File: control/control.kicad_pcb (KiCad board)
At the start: 2 copper layers, 100 x 50 mm, 46 parts, among them J1 Conn_01x06_Male, J2 Conn_01x02_Male, Q1 TD9944, Q2 TD9944, Q3 TD9944, SW1 SW_SPST_X3, U1 Teensy_LC, U2 MCP3208, U3 74HC14

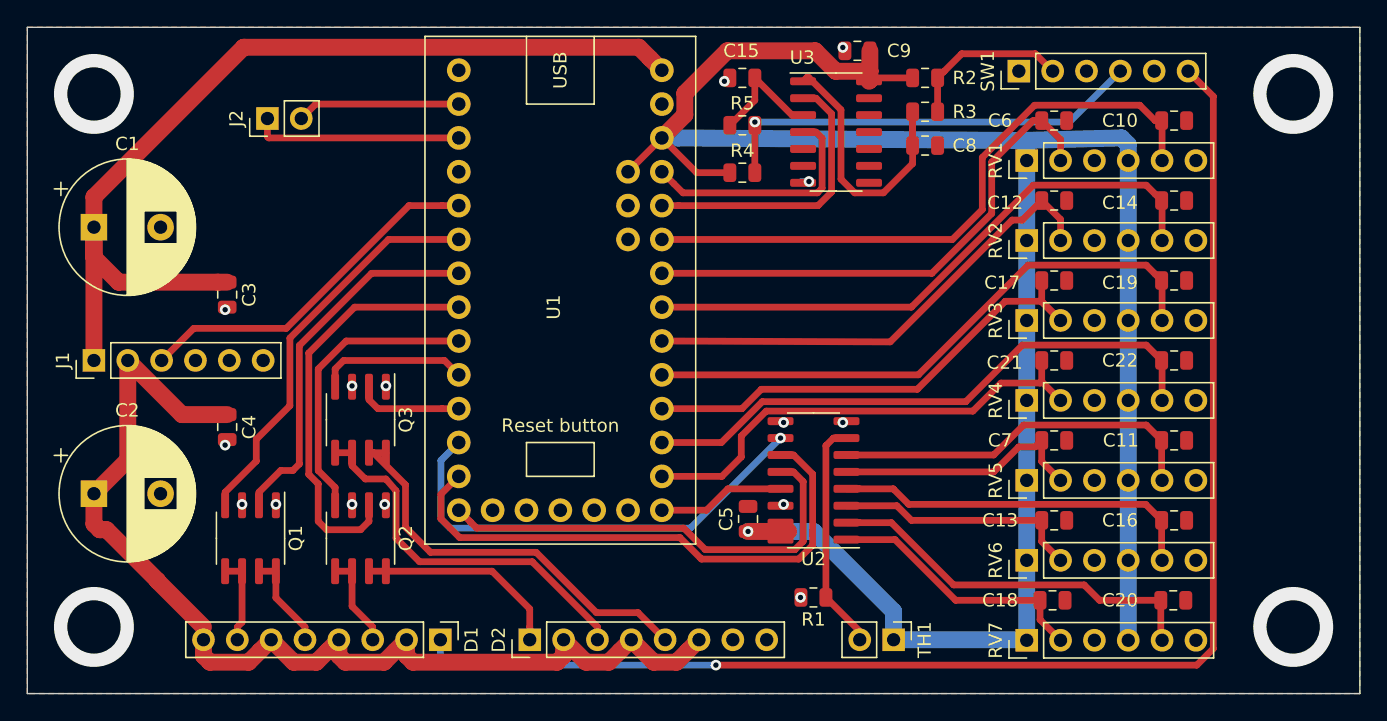
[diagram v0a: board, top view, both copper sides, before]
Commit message: Correction de pad non connecté
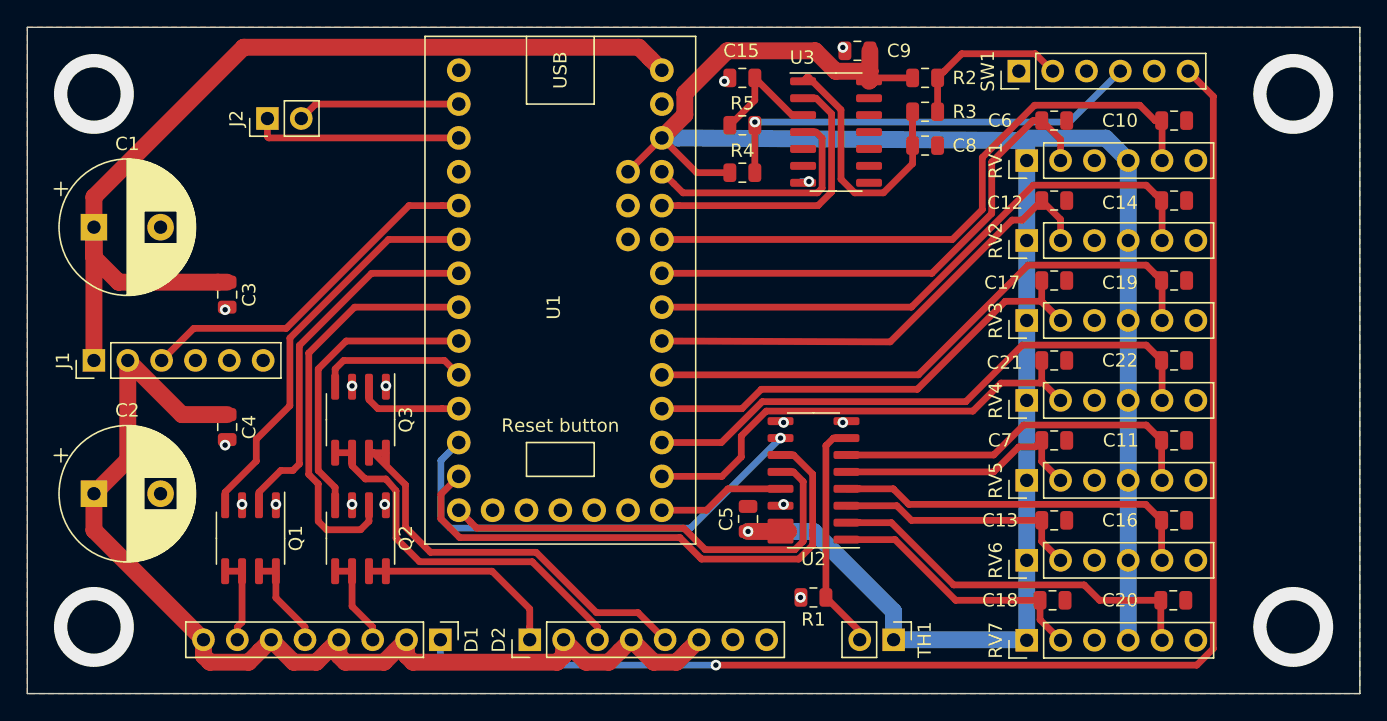
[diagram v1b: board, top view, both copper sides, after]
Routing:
- net D+12V: track 82.3 -> 82.9 mm
- net /MCU/3V3: track 174.1 -> 174.7 mm
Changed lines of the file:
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@@
     (thickness 1.6)
     (drawings 4)
-    (tracks 394)
+    (tracks 391)
     (zones 0)
     (modules 46)
@@
   (via (at 73.025 57.785) (size 0.8) (drill 0.4) (layers F.Cu B.Cu) (net 2))
   (segment (start 73.055 57.785) (end 73.025 57.785) (width 0.508) (layer F.Cu) (net 2))
-  (segment (start 28.22 60) (end 24.765 56.545) (width 1.27) (layer F.Cu) (net 3))
-  (segment (start 24.765 56.545) (end 24.765 56.515) (width 1.27) (layer F.Cu) (net 3))
-  (segment (start 24.765 56.515) (end 20.955 52.705) (width 1.27) (layer F.Cu) (net 3))
-  (segment (start 20 52.27) (end 20 50) (width 1.27) (layer F.Cu) (net 3))
-  (segment (start 20.435 52.705) (end 20 52.27) (width 1.27) (layer F.Cu) (net 3))
-  (segment (start 20.955 52.705) (end 20.435 52.705) (width 1.27) (layer F.Cu) (net 3))
   (segment (start 22.54 47.46) (end 22.54 40) (width 1.27) (layer F.Cu) (net 3))
   (segment (start 20 50) (end 22.54 47.46) (width 1.27) (layer F.Cu) (net 3))
@@
   (segment (start 63.719999 62.645001) (end 64.555001 61.809999) (width 1.27) (layer F.Cu) (net 3))
   (segment (start 60.325 60.96) (end 62.010001 62.645001) (width 1.27) (layer F.Cu) (net 3))
-  (segment (start 92.54 23.415) (end 91.125 22) (width 0.508) (layer F.Cu) (net 4))
-  (segment (start 92.54 25) (end 92.54 23.415) (width 0.508) (layer F.Cu) (net 4))
+  (segment (start 20 52.74) (end 20 50) (width 1.27) (layer F.Cu) (net 3))
+  (segment (start 28.22 60.96) (end 20 52.74) (width 1.27) (layer F.Cu) (net 3))
   (segment (start 91.125 22) (end 90.482798 22) (width 0.508) (layer F.Cu) (net 4))
   (segment (start 87.376 25.106798) (end 87.376 28.970724) (width 0.508) (layer F.Cu) (net 4))
@@
   (segment (start 82.886724 33.46) (end 62.62 33.46) (width 0.508) (layer F.Cu) (net 4))
   (segment (start 87.376 28.970724) (end 82.886724 33.46) (width 0.508) (layer F.Cu) (net 4))
+  (segment (start 92.54 23.415) (end 91.125 22) (width 0.508) (layer F.Cu) (net 4))
+  (segment (start 92.54 25) (end 92.54 23.415) (width 0.508) (layer F.Cu) (net 4))
   (segment (start 90.639473 46.485527) (end 89.404473 46.485527) (width 0.508) (layer F.Cu) (net 5))
   (segment (start 91.125 46) (end 90.639473 46.485527) (width 0.508) (layer F.Cu) (net 5))
@@
   (segment (start 97.62 31) (end 97.62 25) (width 1.27) (layer B.Cu) (net 51))
   (segment (start 63.877235 23.3) (end 62.62 23.3) (width 1.27) (layer B.Cu) (net 51))
-  (segment (start 97.62 23.797919) (end 97.122081 23.3) (width 1.27) (layer B.Cu) (net 51))
-  (segment (start 97.62 25) (end 97.62 23.797919) (width 1.27) (layer B.Cu) (net 51))
   (segment (start 90 23.96) (end 89.535 23.495) (width 1.27) (layer B.Cu) (net 51))
   (segment (start 90 25) (end 90 23.96) (width 1.27) (layer B.Cu) (net 51))
-  (segment (start 97.122081 23.3) (end 89.535 23.495) (width 1.27) (layer B.Cu) (net 51))
   (segment (start 89.535 23.495) (end 63.877235 23.3) (width 1.27) (layer B.Cu) (net 51))
   (segment (start 60.08 25.84) (end 62.62 23.3) (width 0.508) (layer F.Cu) (net 51))
@@
   (segment (start 78.22099 18.29901) (end 78.232 18.288) (width 1.27) (layer F.Cu) (net 51))
   (segment (start 78.232 16.764) (end 78.232 18.288) (width 1.27) (layer F.Cu) (net 51))
+  (segment (start 89.715001 23.314999) (end 89.535 23.495) (width 1.27) (layer B.Cu) (net 51))
+  (segment (start 95.934999 23.314999) (end 89.715001 23.314999) (width 1.27) (layer B.Cu) (net 51))
+  (segment (start 97.62 25) (end 95.934999 23.314999) (width 1.27) (layer B.Cu) (net 51))
+  (segment (start 71.525 52.175) (end 71.525 53.445) (width 0.508) (layer F.Cu) (net 51))
   (segment (start 63.508999 26.728999) (end 62.62 25.84) (width 0.508) (layer F.Cu) (net 53))
   (segment (start 64.20401 27.42401) (end 63.508999 26.728999) (width 0.508) (layer F.Cu) (net 53))

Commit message: Correciton du PCB (espacements entre les connecteurs et polygon pour pour l'ADC.)
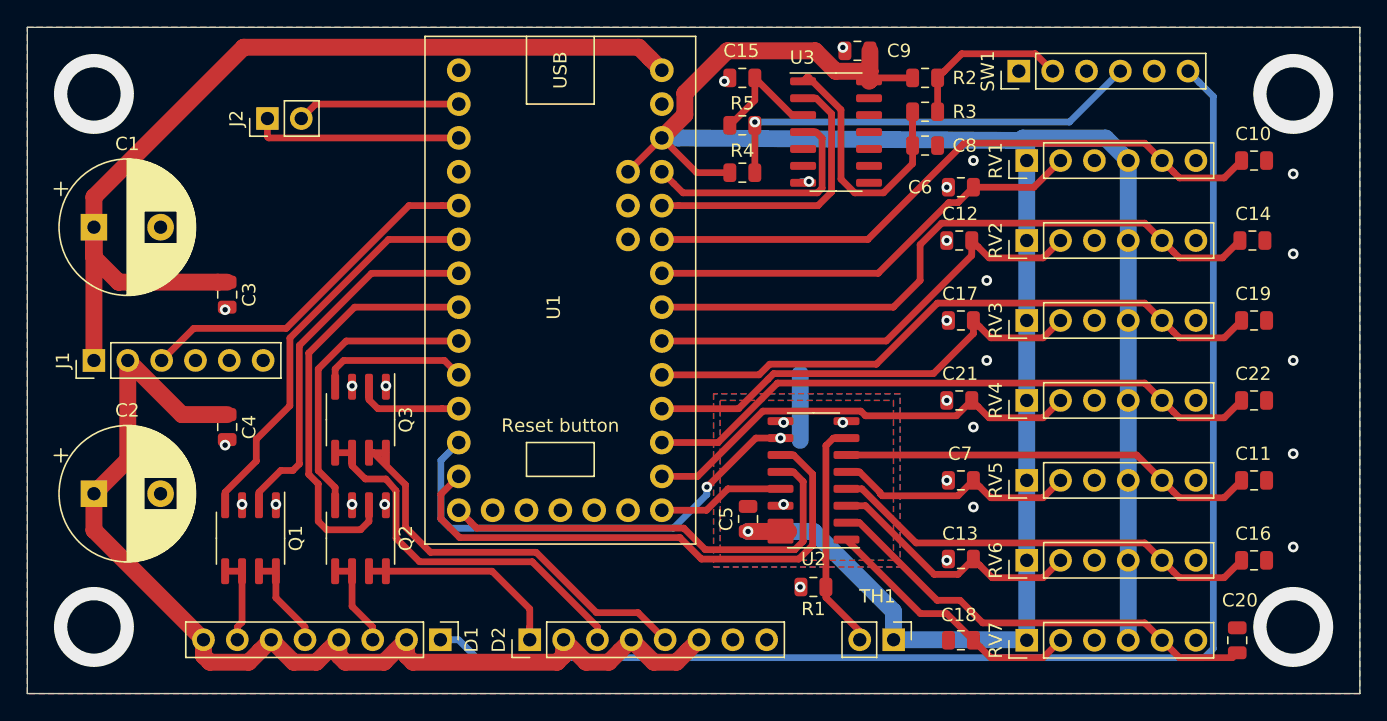
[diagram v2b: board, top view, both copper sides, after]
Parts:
- moved C6 8.60 mm to (85.1, 27.0), turned to 180 degrees
- moved C12 7.73 mm to (84.9, 31.0), turned to 180 degrees
- moved C21 7.73 mm to (84.9, 43.0), turned to 180 degrees
- moved C17 7.62 mm to (85.1, 37.0), turned to 180 degrees
- moved C7 7.62 mm to (85.1, 49.0), turned to 180 degrees
- moved C13 7.58 mm to (85.1, 54.9), turned to 180 degrees
- moved C18 7.50 mm to (85.1, 61.0), turned to 180 degrees
- moved C10 6.71 mm to (107.1, 25.0)
- moved C11 6.71 mm to (107.1, 49.0)
- moved C16 6.71 mm to (107.1, 55.0)
- moved C19 6.71 mm to (107.1, 37.0)
- moved C22 6.71 mm to (107.1, 43.0)
- moved C14 6.60 mm to (106.9, 31.0)
- moved C20 5.66 mm to (105.8, 61.0), turned to 90 degrees
- moved R1 0.78 mm to (74.0, 57.0)
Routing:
- net /MCU/MCU_control_elements/contour_pot: track 39.1 -> 33.4 mm
- net GNDD: track 3.96 -> 9.53 mm, vias 15 -> 31
- net /MCU/MCU_control_elements/octaver_up_pot: track 27.6 -> 33.0 mm
- net /MCU/MCU_control_elements/reverb_vol_pot: track 29.0 -> 33.7 mm
- net /MCU/MCU_control_elements/EQ_low_mid_pot: track 44.8 -> 49.2 mm
- net /MCU/MCU_control_elements/overdrive_tone_pot: track 28.1 -> 31.5 mm
- net /MCU/MCU_control_elements/EQ_high_mid_pot: track 37.4 -> 34.3 mm
- net /MCU/MCU_control_elements/comp_threshold_pot: track 44.0 -> 47.0 mm
- net /MCU/MCU_control_elements/EQ_high_pot: track 44.4 -> 47.4 mm
- net /MCU/MCU_control_elements/comp_ratio_pot: track 36.0 -> 33.7 mm
- net /MCU/MCU_control_elements/EQ_low_pot: track 36.5 -> 34.8 mm
- net Net-(D1-Pad1): track 104.2 -> 103.0 mm, vias 1 -> 0
- net /MCU/MCU_control_elements/octaver_down_pot: track 18.7 -> 19.8 mm
- net /MCU/MCU_control_elements/overdrive_gain_pot: track 19.2 -> 18.4 mm
- net /MCU/MCU_control_elements/presence_pot: track 47.5 -> 48.1 mm
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
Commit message: Ajout du connecteur pour la footswitch.
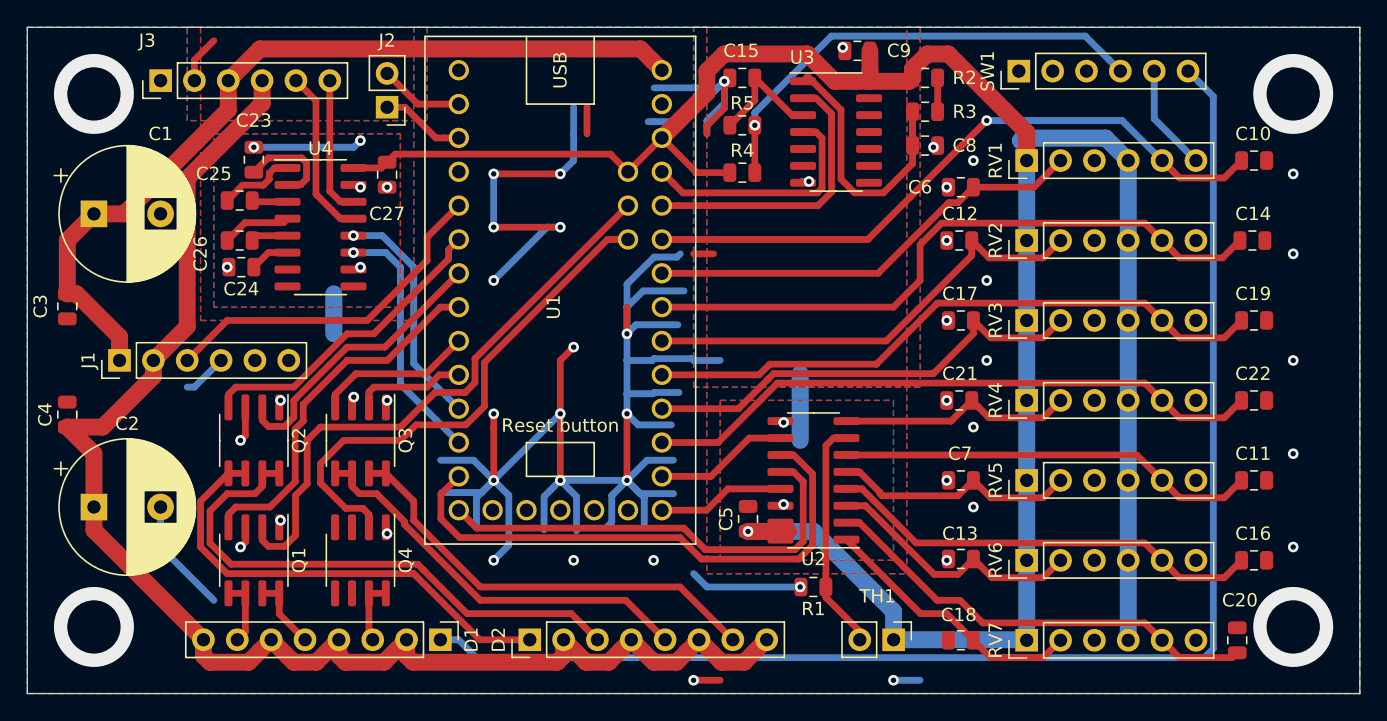
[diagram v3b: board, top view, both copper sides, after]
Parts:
- added C23: 0.1µF, Capacitor_SMD:C_0805_2012Metric, F.Cu at (32.0, 24.9)
- added C24: 0.1µF, Capacitor_SMD:C_0805_2012Metric, F.Cu at (31.1, 33.0)
- added C25: 0.1µF, Capacitor_SMD:C_0805_2012Metric, F.Cu at (30.9, 28.0)
- added C26: 0.1µF, Capacitor_SMD:C_0805_2012Metric, F.Cu at (30.9, 31.0)
- added C27: 0.1µF, Capacitor_SMD:C_0805_2012Metric, F.Cu at (42.0, 26.1)
- added J3: Conn_01x06_Male, Connector_PinHeader_2.54mm:PinHeader_1x06_P2.54mm_Vertical, F.Cu at (25.0, 19.0)
- added Q4: TD9944, Package_SO:SOIC-8_3.9x4.9mm_P1.27mm, F.Cu at (40.0, 55.0)
- added U4: MAX3232, Package_SO:SOIC-16_3.9x9.9mm_P1.27mm, F.Cu at (37.0, 30.0)
- moved C4 12.0 mm to (18.0, 44.1), turned to 90 degrees
- moved C3 12.0 mm to (18.0, 35.9)
- moved Q2 10.9 mm to (32.0, 46.0)
- moved J2 9.02 mm to (42.0, 21.0), turned to 180 degrees
- moved J1 1.92 mm to (21.9, 40.0)
- moved Q1 1.68 mm to (32.0, 55.0)
- moved Q3 1.55 mm to (40.0, 46.0)
- moved C1 1.00 mm to (20.0, 29.0)
- moved C2 1.00 mm to (20.0, 51.0)
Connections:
- D2 pad 7: (no net) -> Net-(D2-Pad7)
- D2 pad 8: (no net) -> D+12V
- Q1 pad 2: /MCU/MCU_LED/comp_LED -> /MCU/comp_LED
- Q2 pad 2: /MCU/MCU_LED/octaver_LED -> /MCU/MCU_LED/delay_LED
- Q2 pad 4: /MCU/MCU_LED/mute_LED -> /MCU/MCU_LED/octaver_LED
- Q2 pad 5: Net-(D1-Pad3) -> Net-(D2-Pad1)
- Q2 pad 6: Net-(D1-Pad3) -> Net-(D2-Pad1)
- Q2 pad 7: Net-(D2-Pad1) -> Net-(D2-Pad3)
- Q2 pad 8: Net-(D2-Pad1) -> Net-(D2-Pad3)
- Q3 pad 2: /MCU/MCU_LED/reverb_LED -> /MCU/MCU_LED/clipping_LED
- Q3 pad 4: /MCU/MCU_LED/delay_LED -> /MCU/MCU_LED/reverb_LED
- Q3 pad 5: Net-(D2-Pad3) -> Net-(D2-Pad5)
- Q3 pad 6: Net-(D2-Pad3) -> Net-(D2-Pad5)
- Q3 pad 7: Net-(D2-Pad5) -> Net-(D2-Pad7)
- Q3 pad 8: Net-(D2-Pad5) -> Net-(D2-Pad7)
- U1 pad 10: /MCU/ADC_CS -> /MCU/FS_TX
- U1 pad 14: /MCU/MCU_control_elements/comp_ratio_pot -> /MCU/ADC_CS
- U1 pad 24: Net-(U1-Pad24) -> /MCU/comp_LED
- U1 pad 25: Net-(U1-Pad25) -> /MCU/mute_LED
- U1 pad 4: /MCU/MCU_LED/overdrive_LED -> /MCU/MCU_LED/octaver_LED
- U1 pad 5: /MCU/MCU_LED/comp_LED -> /MCU/MCU_LED/delay_LED
- U1 pad 6: /MCU/MCU_LED/octaver_LED -> /MCU/MCU_LED/overdrive_LED
- U1 pad 7: /MCU/MCU_LED/mute_LED -> /MCU/MCU_LED/reverb_LED
- U1 pad 8: /MCU/MCU_LED/delay_LED -> /MCU/MCU_LED/clipping_LED
- U1 pad 9: /MCU/MCU_LED/reverb_LED -> /MCU/FS_RX
- U2 pad 8: GNDD -> /MCU/MCU_control_elements/comp_ratio_pot
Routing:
- net GNDD: track 9.53 -> 232.2 mm, vias 31 -> 54
- net /MCU/comp_LED: track 0.00 -> 43.9 mm
- net /MCU/mute_LED: track 0.00 -> 39.0 mm
- net Net-(D2-Pad7): track 0.00 -> 33.3 mm
- net /MCU/MCU_LED/comp_LED: track 28.0 -> 0.00 mm
- net D+12V: track 82.9 -> 108.7 mm
- net /MCU/ADC_CS: track 35.2 -> 10.1 mm, vias 2 -> 0
- net /MCU/MCU_LED/mute_LED: track 22.2 -> 0.00 mm
- net Net-(D2-Pad1): track 15.6 -> 35.3 mm
- net /MCU/FS_TX: track 0.00 -> 19.0 mm, vias 0 -> 1
- net /MCU/FS_RX: track 0.00 -> 17.5 mm, vias 0 -> 1
- net /MCU/MCU_control_elements/comp_ratio_pot: track 33.7 -> 17.8 mm
- net Net-(J3-Pad5): track 0.00 -> 12.7 mm
- net Net-(D2-Pad3): track 28.8 -> 41.4 mm
- net Net-(J3-Pad6): track 0.00 -> 10.4 mm
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
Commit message: Ajout du projet et de la schématique de footswitch
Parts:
- added REF**: MountingHole_3.2mm_M3, MountingHole:MountingHole_3.2mm_M3, F.Cu at (110.0, 20.0)
- added REF**: MountingHole_3.2mm_M3, MountingHole:MountingHole_3.2mm_M3, F.Cu at (110.0, 60.0)
- added REF**: MountingHole_3.2mm_M3, MountingHole:MountingHole_3.2mm_M3, F.Cu at (20.0, 20.0)
- added REF**: MountingHole_3.2mm_M3, MountingHole:MountingHole_3.2mm_M3, F.Cu at (20.0, 60.0)
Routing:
- net (no net): vias 4 -> 0

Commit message: Ajout du gnd pour le RX/TX du DSP
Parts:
- added J4: Conn_01x01_Male, Connector_PinHeader_2.54mm:PinHeader_1x01_P2.54mm_Vertical, F.Cu at (27.0, 45.0)
- D1, D2: value LED_PAD -> LED
- J2: value Conn_01x02_Male -> Conn_01x03_Male; footprint Connector_PinHeader_2.54mm:PinHeader_1x02_P2.54mm_Vertical -> Connector_PinHeader_2.54mm:PinHeader_1x03_P2.54mm_Vertical; moved to B.Cu
- J3: value Conn_01x06_Male -> footswitch
- moved J2 15.2 mm to (57.1, 19.0), turned to 90 degrees
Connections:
- J2 pad 1: /MCU/DSP_RX -> GNDD
- J2 pad 2: /MCU/DSP_TX -> /MCU/DSP_RX
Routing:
- net /MCU/DSP_RX: track 6.33 -> 8.94 mm
- net /MCU/DSP_TX: track 6.33 -> 5.35 mm

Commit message: Finalisation du PCB de la footswitch. Correction de la position des mounting holes.
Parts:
- removed J4: Conn_01x01_Male, Connector_PinHeader_2.54mm:PinHeader_1x01_P2.54mm_Vertical
- removed the REF** at (110.0, 20.0)
- removed the REF** at (20.0, 20.0)
- removed the REF** at (20.0, 60.0)
- added REF**: MountingHole_3.2mm_M3, MountingHole:MountingHole_3.2mm_M3, F.Cu at (111.0, 19.0)
- added REF**: MountingHole_3.2mm_M3, MountingHole:MountingHole_3.2mm_M3, F.Cu at (19.0, 19.0)
- added REF**: MountingHole_3.2mm_M3, MountingHole:MountingHole_3.2mm_M3, F.Cu at (19.0, 61.0)
- moved REF** 1.41 mm to (111.0, 61.0)
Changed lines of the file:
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@@
     (tracks 641)
     (zones 0)
-    (modules 59)
+    (modules 58)
     (nets 68)
   )
@@
   )
   (setup
-    (last_trace_width 0.508)
+    (last_trace_width 0.25)
     (user_trace_width 0.254)
     (user_trace_width 0.381)
@@
     )
   )
-  (module Connector_PinHeader_2.54mm:PinHeader_1x01_P2.54mm_Vertical (layer F.Cu)
-    (at 27 45)
-    (descr "Through hole straight pin header, 1x01, 2.54mm pitch, single row")
-    (tags "Through hole pin header THT 1x01 2.54mm single row")
-    (fp_text reference J4 (at 0 -2.33) (layer F.SilkS)
-      (effects (font (size 1 1) (thickness 0.15)))
-    )
-    (fp_text value Conn_01x01_Male (at 0 2.33) (layer F.Fab)
-      (effects (font (size 1 1) (thickness 0.15)))
-    )
-    (fp_text user %R (at 0 0 90) (layer F.Fab)
-      (effects (font (size 1 1) (thickness 0.15)))
-    )
-    (fp_line (start 1.8 -1.8) (end -1.8 -1.8) (layer F.CrtYd) (width 0.05))
-    (fp_line (start 1.8 1.8) (end 1.8 -1.8) (layer F.CrtYd) (width 0.05))
-    (fp_line (start -1.8 1.8) (end 1.8 1.8) (layer F.CrtYd) (width 0.05))
-    (fp_line (start -1.8 -1.8) (end -1.8 1.8) (layer F.CrtYd) (width 0.05))
-    (fp_line (start -1.33 -1.33) (end 0 -1.33) (layer F.SilkS) (width 0.12))
-    (fp_line (start -1.33 0) (end -1.33 -1.33) (layer F.SilkS) (width 0.12))
-    (fp_line (start -1.33 1.27) (end 1.33 1.27) (layer F.SilkS) (width 0.12))
-    (fp_line (start 1.33 1.27) (end 1.33 1.33) (layer F.SilkS) (width 0.12))
-    (fp_line (start -1.33 1.27) (end -1.33 1.33) (layer F.SilkS) (width 0.12))
-    (fp_line (start -1.33 1.33) (end 1.33 1.33) (layer F.SilkS) (width 0.12))
-    (fp_line (start -1.27 -0.635) (end -0.635 -1.27) (layer F.Fab) (width 0.1))
-    (fp_line (start -1.27 1.27) (end -1.27 -0.635) (layer F.Fab) (width 0.1))
-    (fp_line (start 1.27 1.27) (end -1.27 1.27) (layer F.Fab) (width 0.1))
-    (fp_line (start 1.27 -1.27) (end 1.27 1.27) (layer F.Fab) (width 0.1))
-    (fp_line (start -0.635 -1.27) (end 1.27 -1.27) (layer F.Fab) (width 0.1))
-    (pad 1 thru_hole rect (at 0 0) (size 1.7 1.7) (drill 1) (layers *.Cu *.Mask)
-      (net 2 GNDD))
-    (model ${KISYS3DMOD}/Connector_PinHeader_2.54mm.3dshapes/PinHeader_1x01_P2.54mm_Vertical.wrl
-      (at (xyz 0 0 0))
-      (scale (xyz 1 1 1))
-      (rotate (xyz 0 0 0))
-    )
-  )
   (module MountingHole:MountingHole_3.2mm_M3 (layer F.Cu)
-    (at 110 20)
+    (at 111 19)
     (descr "Mounting Hole 3.2mm, no annular, M3")
     (tags "mounting hole 3.2mm no annular m3")
@@
   )
   (module MountingHole:MountingHole_3.2mm_M3 (layer F.Cu)
-    (at 110 60)
+    (at 111 61)
     (descr "Mounting Hole 3.2mm, no annular, M3")
     (tags "mounting hole 3.2mm no annular m3")
@@
   )
   (module MountingHole:MountingHole_3.2mm_M3 (layer F.Cu)
-    (at 20 20)
+    (at 19 19)
     (descr "Mounting Hole 3.2mm, no annular, M3")
     (tags "mounting hole 3.2mm no annular m3")
@@
   )
   (module MountingHole:MountingHole_3.2mm_M3 (layer F.Cu)
-    (at 20 60)
+    (at 19 61)
     (descr "Mounting Hole 3.2mm, no annular, M3")
     (tags "mounting hole 3.2mm no annular m3")
